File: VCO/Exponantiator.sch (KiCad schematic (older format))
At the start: 14 parts

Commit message: New PCB
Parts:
- removed Q? (x2): MMDT3904, Package_TO_SOT_SMD:SOT-363_SC-70-6, symbol Transistor_BJT:MMDT3904
- added Q401: DMMT3904, Package_TO_SOT_SMD:SOT-363_SC-70-6, symbol telec:DMMT3904
- RV401: renamed from RV?; footprint Potentiometer_THT:Potentiometer_Bourns_3299W_Vertical -> Potentiometer_THT:Potentiometer_Bourns_3296W_Vertical
- gave numbers to parts that had none: 9
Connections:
- net CV: now also Q401.2 (B2)
- net GND: now also Q401.1 (B2)
- net at C404.2, R402.1, U401.6 (-): now also Q401.3 (C2)
- net at R404.2: now also Q401.4 (E2), Q401.5 (E2)
- net at C403.2, R401.2, U401.2 (-): now also Q401.6 (C2)
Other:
- moved on the sheet: R403
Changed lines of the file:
@@
 $EndDescr
 $Comp
-L Device:C C?
+L Device:C C404
 U 1 1 5FB1B0B6
 P 1500 3600
-F 0 "C?" V 1600 3500 50  0000 C CNN
+F 0 "C404" V 1350 3600 50  0000 C CNN
 F 1 "1n" V 1600 3700 50  0000 C CNN
 F 2 "Capacitor_THT:C_Disc_D7.0mm_W2.5mm_P5.00mm" H 1538 3450 50  0001 C CNN
@@
 $EndComp
 $Comp
-L power:-12V #PWR?
+L power:-12V #PWR0403
 U 1 1 5FB1B0BC
 P 2100 1050
-F 0 "#PWR?" H 2100 1150 50  0001 C CNN
+F 0 "#PWR0403" H 2100 1150 50  0001 C CNN
 F 1 "-12V" H 2115 1223 50  0000 C CNN
 F 2 "" H 2100 1050 50  0001 C CNN
@@
 $EndComp
 $Comp
-L power:GND #PWR?
+L power:GND #PWR0410
 U 1 1 5FB1B0C2
 P 1150 4200
-F 0 "#PWR?" H 1150 3950 50  0001 C CNN
+F 0 "#PWR0410" H 1150 3950 50  0001 C CNN
 F 1 "GND" H 1155 4027 50  0000 C CNN
 F 2 "" H 1150 4200 50  0001 C CNN
@@
 $EndComp
 $Comp
-L Transistor_BJT:MMDT3904 Q?
-U 1 1 5FB1B0C8
-P 1600 2900
-F 0 "Q?" H 1750 3000 50  0000 L CNN
-F 1 "MMDT3904" H 1300 3050 50  0000 L CNN
-F 2 "Package_TO_SOT_SMD:SOT-363_SC-70-6" H 1800 3000 50  0001 C CNN
-F 3 "http://www.diodes.com/_files/datasheets/ds30088.pdf" H 1600 2900 50  0001 C CNN
-	1    1600 2900
-	1    0    0    -1
-$EndComp
-$Comp
-L Transistor_BJT:MMDT3904 Q?
-U 2 1 5FB1B0CE
-P 2200 2900
-F 0 "Q?" H 2350 2800 50  0000 L CNN
-F 1 "MMDT3904" H 1850 3050 50  0000 L CNN
-F 2 "Package_TO_SOT_SMD:SOT-363_SC-70-6" H 2400 3000 50  0001 C CNN
-F 3 "http://www.diodes.com/_files/datasheets/ds30088.pdf" H 2200 2900 50  0001 C CNN
-	2    2200 2900
-	-1   0    0    -1
-$EndComp
-$Comp
-L Amplifier_Operational:TL082 U?
+L Amplifier_Operational:TL082 U401
 U 1 1 5FB1B0D4
 P 3050 2600
-F 0 "U?" H 3250 2400 50  0000 C CNN
-F 1 "TL082" H 3250 2500 50  0000 C CNN
+F 0 "U401" H 3250 2800 50  0000 C CNN
+F 1 "TL082" H 3250 2700 50  0000 C CNN
 F 2 "Package_DIP:DIP-8_W7.62mm_LongPads" H 3050 2600 50  0001 C CNN
 F 3 "http://www.ti.com/lit/ds/symlink/tl081.pdf" H 3050 2600 50  0001 C CNN
@@
 $EndComp
 $Comp
-L Device:R_POT_TRIM RV?
+L Device:R_POT_TRIM RV401
 U 1 1 5FB1B0DA
 P 3200 2200
-F 0 "RV?" V 3300 2350 50  0000 C CNN
+F 0 "RV401" V 3100 2200 50  0000 C CNN
 F 1 "10k" V 3200 2200 50  0000 C CNN
-F 2 "Potentiometer_THT:Potentiometer_Bourns_3299W_Vertical" H 3200 2200 50  0001 C CNN
+F 2 "Potentiometer_THT:Potentiometer_Bourns_3296W_Vertical" H 3200 2200 50  0001 C CNN
 F 3 "~" H 3200 2200 50  0001 C CNN
 	1    3200 2200
@@
 	1150 3600 1350 3600
 $Comp
-L Device:R R?
+L Device:R R404
 U 1 1 5FB1B0E8
 P 1900 3350
-F 0 "R?" V 2000 3350 50  0000 C CNN
+F 0 "R404" V 2000 3350 50  0000 C CNN
 F 1 "1k" V 1900 3350 50  0000 C CNN
 F 2 "Resistor_THT:R_Axial_DIN0204_L3.6mm_D1.6mm_P7.62mm_Horizontal" V 1830 3350 50  0001 C CNN
@@
 $EndComp
 $Comp
-L power:GND #PWR?
+L power:GND #PWR0409
 U 1 1 5FB1B0EE
 P 2500 3000
-F 0 "#PWR?" H 2500 2750 50  0001 C CNN
+F 0 "#PWR0409" H 2500 2750 50  0001 C CNN
 F 1 "GND" H 2505 2827 50  0000 C CNN
 F 2 "" H 2500 3000 50  0001 C CNN
@@
 Connection ~ 1900 3600
 $Comp
-L Device:R R?
+L Device:R R402
 U 1 1 5FB1B0FE
 P 1700 2400
-F 0 "R?" V 1800 2400 50  0000 C CNN
+F 0 "R402" V 1800 2400 50  0000 C CNN
 F 1 "1M" V 1700 2400 50  0000 C CNN
 F 2 "Resistor_THT:R_Axial_DIN0204_L3.6mm_D1.6mm_P7.62mm_Horizontal" V 1630 2400 50  0001 C CNN
@@
 $EndComp
 $Comp
-L power:+12V #PWR?
+L power:+12V #PWR0407
 U 1 1 5FB1B104
 P 1700 2250
-F 0 "#PWR?" H 1700 2100 50  0001 C CNN
+F 0 "#PWR0407" H 1700 2100 50  0001 C CNN
 F 1 "+12V" H 1715 2423 50  0000 C CNN
 F 2 "" H 1700 2250 50  0001 C CNN
@@
 	2600 2500 2600 2200
 $Comp
-L power:GND #PWR?
+L power:GND #PWR0408
 U 1 1 5FB1B117
 P 2700 2800
-F 0 "#PWR?" H 2700 2550 50  0001 C CNN
+F 0 "#PWR0408" H 2700 2550 50  0001 C CNN
 F 1 "GND" H 2705 2627 50  0000 C CNN
 F 2 "" H 2700 2800 50  0001 C CNN
@@
 	2700 2700 2750 2700
 $Comp
-L Device:R R?
+L Device:R R401
 U 1 1 5FB1B11F
 P 2850 2200
-F 0 "R?" V 2750 2200 50  0000 C CNN
+F 0 "R401" V 2750 2200 50  0000 C CNN
 F 1 "22k" V 2850 2200 50  0000 C CNN
 F 2 "Resistor_THT:R_Axial_DIN0204_L3.6mm_D1.6mm_P7.62mm_Horizontal" V 2780 2200 50  0001 C CNN
@@
 Connection ~ 2600 2500
 Wire Wire Line
-	3800 2600 4100 2600
-$Comp
-L Device:C C?
+	3850 2600 4100 2600
+$Comp
+L Device:C C401
 U 1 1 5FB1B12E
 P 1750 1200
-F 0 "C?" V 1850 1100 50  0000 C CNN
-F 1 "100n" V 1850 1300 50  0000 C CNN
+F 0 "C401" H 1900 1300 50  0000 C CNN
+F 1 "100n" H 1900 1100 50  0000 C CNN
 F 2 "Capacitor_SMD:C_0805_2012Metric_Pad1.15x1.40mm_HandSolder" H 1788 1050 50  0001 C CNN
 F 3 "~" H 1750 1200 50  0001 C CNN
@@
 $EndComp
 $Comp
-L power:+12V #PWR?
+L power:+12V #PWR0402
 U 1 1 5FB1B134
 P 1750 1050
-F 0 "#PWR?" H 1750 900 50  0001 C CNN
+F 0 "#PWR0402" H 1750 900 50  0001 C CNN
 F 1 "+12V" H 1765 1223 50  0000 C CNN
 F 2 "" H 1750 1050 50  0001 C CNN
@@
 $EndComp
 $Comp
-L power:GND #PWR?
+L power:GND #PWR0404
 U 1 1 5FB1B13A
 P 1750 1350
-F 0 "#PWR?" H 1750 1100 50  0001 C CNN
+F 0 "#PWR0404" H 1750 1100 50  0001 C CNN
 F 1 "GND" H 1755 1177 50  0000 C CNN
 F 2 "" H 1750 1350 50  0001 C CNN
@@
 $EndComp
 $Comp
-L Device:C C?
+L Device:C C402
 U 1 1 5FB1B140
 P 2100 1200
-F 0 "C?" V 2200 1100 50  0000 C CNN
-F 1 "100n" V 2200 1300 50  0000 C CNN
+F 0 "C402" H 2250 1300 50  0000 C CNN
+F 1 "100n" H 2250 1100 50  0000 C CNN
 F 2 "Capacitor_SMD:C_0805_2012Metric_Pad1.15x1.40mm_HandSolder" H 2138 1050 50  0001 C CNN
 F 3 "~" H 2100 1200 50  0001 C CNN
@@
 $EndComp
 $Comp
-L power:GND #PWR?
+L power:GND #PWR0405
 U 1 1 5FB1B146
 P 2100 1350
-F 0 "#PWR?" H 2100 1100 50  0001 C CNN
+F 0 "#PWR0405" H 2100 1100 50  0001 C CNN
 F 1 "GND" H 2105 1177 50  0000 C CNN
 F 2 "" H 2100 1350 50  0001 C CNN
@@
 $EndComp
 $Comp
-L Amplifier_Operational:TL082 U?
+L Amplifier_Operational:TL082 U401
 U 3 1 5FB1B14C
 P 1350 1200
-F 0 "U?" H 1550 1000 50  0000 C CNN
+F 0 "U401" H 1550 1000 50  0000 C CNN
 F 1 "TL082" H 1550 1100 50  0000 C CNN
 F 2 "Package_DIP:DIP-8_W7.62mm_LongPads" H 1350 1200 50  0001 C CNN
@@
 $EndComp
 $Comp
-L power:+12V #PWR?
+L power:+12V #PWR0401
 U 1 1 5FB1B152
 P 1450 900
-F 0 "#PWR?" H 1450 750 50  0001 C CNN
+F 0 "#PWR0401" H 1450 750 50  0001 C CNN
 F 1 "+12V" H 1465 1073 50  0000 C CNN
 F 2 "" H 1450 900 50  0001 C CNN
@@
 $EndComp
 $Comp
-L power:-12V #PWR?
+L power:-12V #PWR0406
 U 1 1 5FB1B158
 P 1450 1500
-F 0 "#PWR?" H 1450 1600 50  0001 C CNN
+F 0 "#PWR0406" H 1450 1600 50  0001 C CNN
 F 1 "-12V" H 1465 1673 50  0000 C CNN
 F 2 "" H 1450 1500 50  0001 C CNN
@@
 $EndComp
 $Comp
-L Amplifier_Operational:TL082 U?
+L Amplifier_Operational:TL082 U401
 U 2 1 5FB1B15E
 P 1500 4000
-F 0 "U?" H 1700 3800 50  0000 C CNN
-F 1 "TL082" H 1700 3900 50  0000 C CNN
+F 0 "U401" H 1700 4200 50  0000 C CNN
+F 1 "TL082" H 1700 4100 50  0000 C CNN
 F 2 "Package_DIP:DIP-8_W7.62mm_LongPads" H 1500 4000 50  0001 C CNN
 F 3 "http://www.ti.com/lit/ds/symlink/tl081.pdf" H 1500 4000 50  0001 C CNN
@@
 $EndComp
 $Comp
-L Device:C C?
+L Device:C C403
 U 1 1 5FB1B169
 P 3100 1900
-F 0 "C?" V 3200 1800 50  0000 C CNN
-F 1 "220p" V 3200 2000 50  0000 C CNN
+F 0 "C403" V 2950 1900 50  0000 C CNN
+F 1 "220p" V 3200 2050 50  0000 C CNN
 F 2 "Capacitor_THT:C_Disc_D7.0mm_W2.5mm_P5.00mm" H 3138 1750 50  0001 C CNN
 F 3 "~" H 3100 1900 50  0001 C CNN
@@
 	2600 2200 2700 2200
 $Comp
-L Device:R R?
+L Device:R R403
 U 1 1 5FB1B176
-P 3650 2600
-F 0 "R?" V 3750 2600 50  0000 C CNN
-F 1 "0" V 3650 2600 50  0000 C CNN
-F 2 "Resistor_THT:R_Axial_DIN0204_L3.6mm_D1.6mm_P7.62mm_Horizontal" V 3580 2600 50  0001 C CNN
-F 3 "~" H 3650 2600 50  0001 C CNN
-	1    3650 2600
+P 3700 2600
+F 0 "R403" V 3800 2600 50  0000 C CNN
+F 1 "0" V 3700 2600 50  0000 C CNN
+F 2 "Resistor_THT:R_Axial_DIN0204_L3.6mm_D1.6mm_P7.62mm_Horizontal" V 3630 2600 50  0001 C CNN
+F 3 "~" H 3700 2600 50  0001 C CNN
+	1    3700 2600
 	0    1    -1   0
 $EndComp
 Wire Wire Line
-	3500 2600 3450 2600
+	3550 2600 3450 2600
 Connection ~ 3450 2600
 Text HLabel 4100 2600 2    50   Input ~ 0
@@
 Text HLabel 900  2900 0    50   Input ~ 0
 CV
+$Comp
+L telec:DMMT3904 Q401
+U 1 1 600FFB80
+P 1600 2900
+F 0 "Q401" H 1750 3000 50  0000 L CNN
+F 1 "DMMT3904" H 1250 3050 50  0000 L CNN
+F 2 "Package_TO_SOT_SMD:SOT-363_SC-70-6" H 1800 3000 50  0001 C CNN
+F 3 "https://www.mccsemi.com/pdf/Products/DMMT3904(SOT-363).PDF" H 1600 2900 50  0001 C CNN
+	1    1600 2900
+	1    0    0    -1
+$EndComp
+$Comp
+L telec:DMMT3904 Q401
+U 2 1 6010095E
+P 2200 2900
+F 0 "Q401" H 2300 2750 50  0000 L CNN
+F 1 "DMMT3904" H 1800 3050 50  0000 L CNN
+F 2 "Package_TO_SOT_SMD:SOT-363_SC-70-6" H 2400 3000 50  0001 C CNN
+F 3 "https://www.mccsemi.com/pdf/Products/DMMT3904(SOT-363).PDF" H 2200 2900 50  0001 C CNN
+	2    2200 2900
+	-1   0    0    -1
+$EndComp
 $EndSCHEMATC

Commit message: Layout VCO
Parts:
- Q401: footprint Package_TO_SOT_SMD:SOT-363_SC-70-6 -> Package_TO_SOT_SMD:SOT-23-6_Handsoldering
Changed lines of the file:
@@
 F 0 "Q401" H 1750 3000 50  0000 L CNN
 F 1 "DMMT3904" H 1250 3050 50  0000 L CNN
-F 2 "Package_TO_SOT_SMD:SOT-363_SC-70-6" H 1800 3000 50  0001 C CNN
+F 2 "Package_TO_SOT_SMD:SOT-23-6_Handsoldering" H 1800 3000 50  0001 C CNN
 F 3 "https://www.mccsemi.com/pdf/Products/DMMT3904(SOT-363).PDF" H 1600 2900 50  0001 C CNN
 	1    1600 2900
@@
 F 0 "Q401" H 2300 2750 50  0000 L CNN
 F 1 "DMMT3904" H 1800 3050 50  0000 L CNN
-F 2 "Package_TO_SOT_SMD:SOT-363_SC-70-6" H 2400 3000 50  0001 C CNN
+F 2 "Package_TO_SOT_SMD:SOT-23-6_Handsoldering" H 2400 3000 50  0001 C CNN
 F 3 "https://www.mccsemi.com/pdf/Products/DMMT3904(SOT-363).PDF" H 2200 2900 50  0001 C CNN
 	2    2200 2900

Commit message: VCO artwork done
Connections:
- net GND: now also U401.3 (+), U401.5 (+); no longer U401.3 (+), U401.5 (+)
- net at C404.1, R404.1: now also U401.1; no longer U401.7
- net at C404.2, Q401.3 (C2), R402.1: now also U401.2 (-); no longer U401.6 (-)
- net at C403.1, R403.2, RV401.2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: now also U401.7; no longer U401.1
- net at C403.2, Q401.6 (C2), R401.2: now also U401.6 (-); no longer U401.2 (-)
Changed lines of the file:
@@
 $Comp
 L Amplifier_Operational:TL082 U401
-U 1 1 5FB1B0D4
+U 2 1 5FB1B0D4
 P 3050 2600
 F 0 "U401" H 3250 2800 50  0000 C CNN
@@
 F 2 "Package_DIP:DIP-8_W7.62mm_LongPads" H 3050 2600 50  0001 C CNN
 F 3 "http://www.ti.com/lit/ds/symlink/tl081.pdf" H 3050 2600 50  0001 C CNN
-	1    3050 2600
+	2    3050 2600
 	1    0    0    1
 $EndComp
@@
 $Comp
 L Amplifier_Operational:TL082 U401
-U 2 1 5FB1B15E
+U 1 1 5FB1B15E
 P 1500 4000
 F 0 "U401" H 1700 4200 50  0000 C CNN
@@
 F 2 "Package_DIP:DIP-8_W7.62mm_LongPads" H 1500 4000 50  0001 C CNN
 F 3 "http://www.ti.com/lit/ds/symlink/tl081.pdf" H 1500 4000 50  0001 C CNN
-	2    1500 4000
-	1    0    0    1
-$EndComp
+	1    1500 4000
+	1    0    0    1
+$EndComp

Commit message: VCO done
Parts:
- added R404: 0, Resistor_THT:R_Axial_DIN0204_L3.6mm_D1.6mm_P7.62mm_Horizontal, symbol Device:R
- renumbered R404 to R403, R403 to R405
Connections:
- net CV: now also R404.2; no longer Q401.2 (B2)
- new net: Q401.2 (B2), R404.1
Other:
- note added: "With this gain,\nthe circuit saturate with\ninput higher than 200mV.\nMaybe lower the gain ?"
- moved on the sheet: C403, C404, Q401A, Q401B, R401, R402, R403, R405, RV401, U401A, U401B

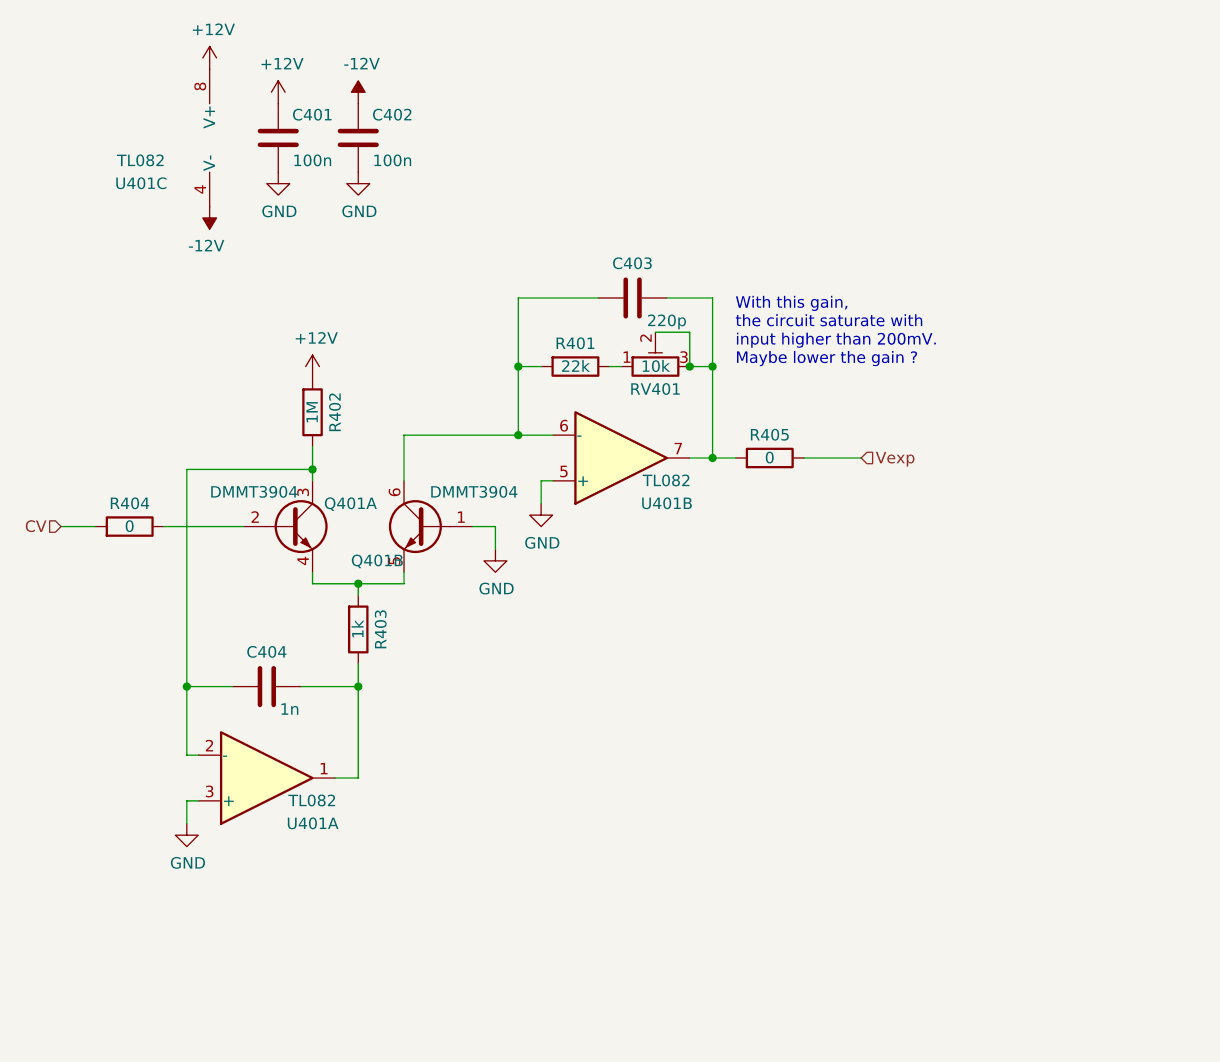
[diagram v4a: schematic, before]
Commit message: Added HF trim, ready to fab
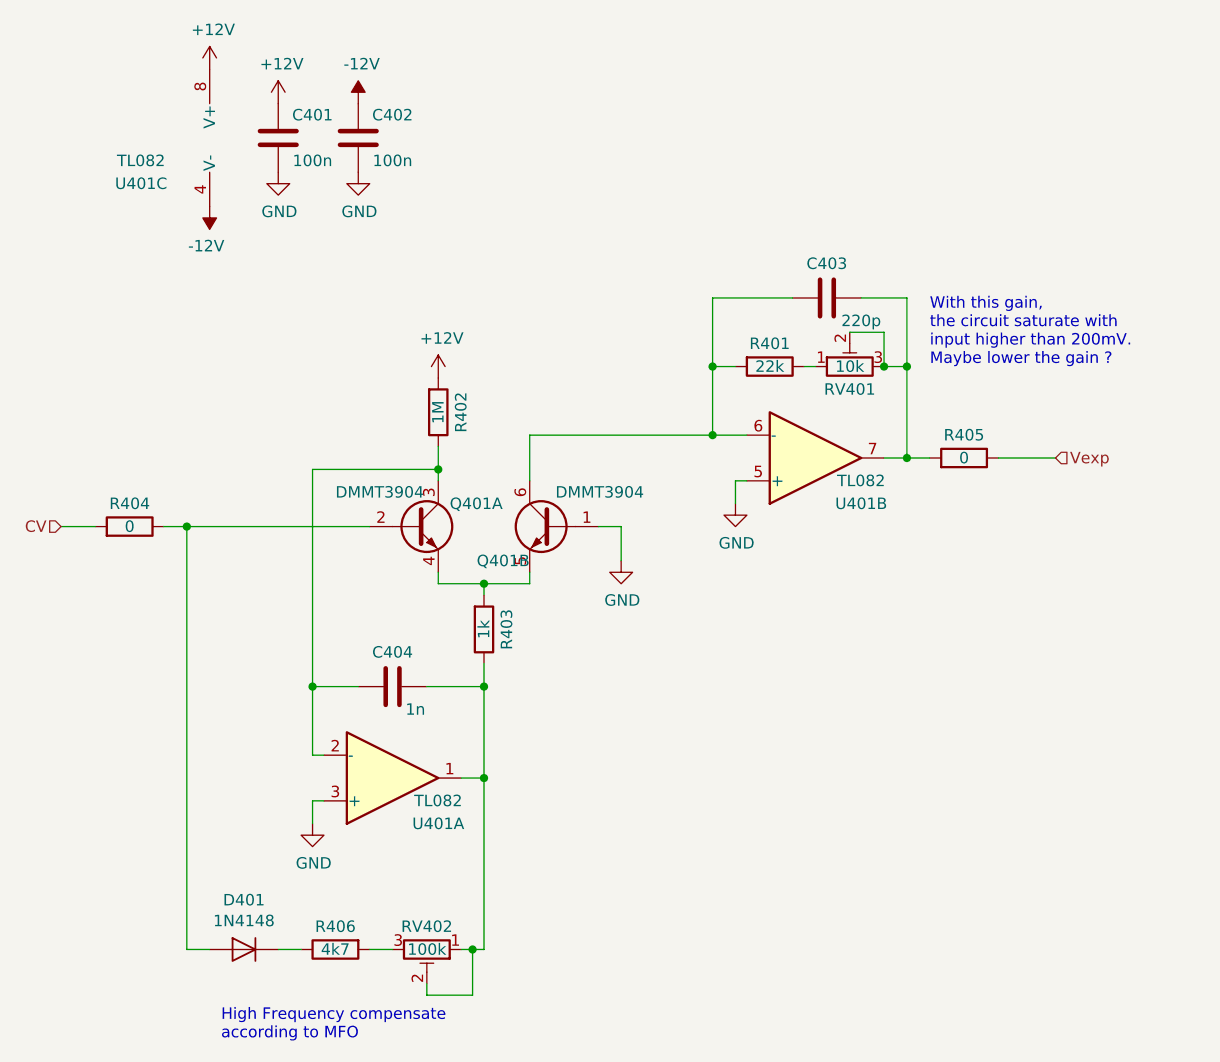
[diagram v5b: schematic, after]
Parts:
- added D401: 1N4148, Diode_THT:D_DO-35_SOD27_P7.62mm_Horizontal, symbol Diode:1N4148
- added R406: 4k7, Resistor_THT:R_Axial_DIN0204_L3.6mm_D1.6mm_P7.62mm_Horizontal, symbol Device:R
- added RV402: 100k, Potentiometer_THT:Potentiometer_Bourns_3296W_Vertical, symbol Device:R_POT_TRIM
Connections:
- net at Q401.2 (B2), R404.1: now also D401.2 (A)
- net at C404.1, R403.1, U401.1: now also RV402.1, RV402.2
- new net: R406.2, RV402.3
- new net: D401.1 (K), R406.1
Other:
- note added: "High Frequency compensate\naccording to MFO"
- moved on the sheet: C403, C404, Q401A, Q401B, R401, R402, R403, R405, RV401, U401A, U401B
